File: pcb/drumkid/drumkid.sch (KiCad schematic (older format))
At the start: 21 parts

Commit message: more schematic stuff
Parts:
- added C? (x2): C, symbol Device:C
- added Y?: Crystal, symbol Device:Crystal
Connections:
- net GND: now also C?.1, C?.1
- net at U?.10 (XTAL2/PB7): now also C?.2, Y?.1
- net at U?.9 (XTAL1/PB6): now also C?.2, Y?.2
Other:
- moved on the sheet: RV?
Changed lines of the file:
@@
 L Device:R_POT RV?
 U 1 1 5C8AAE8E
-P 4950 4000
-F 0 "RV?" H 4880 3954 50  0000 R CNN
-F 1 "R_POT" H 4880 4045 50  0000 R CNN
-F 2 "" H 4950 4000 50  0001 C CNN
-F 3 "~" H 4950 4000 50  0001 C CNN
-	1    4950 4000
+P 6200 4550
+F 0 "RV?" H 6130 4504 50  0000 R CNN
+F 1 "R_POT" H 6130 4595 50  0000 R CNN
+F 2 "" H 6200 4550 50  0001 C CNN
+F 3 "~" H 6200 4550 50  0001 C CNN
+	1    6200 4550
 	-1   0    0    1
 $EndComp
@@
 L power:VCC #PWR?
 U 1 1 5C8AB124
-P 4950 3850
-F 0 "#PWR?" H 4950 3700 50  0001 C CNN
-F 1 "VCC" H 4967 4023 50  0000 C CNN
-F 2 "" H 4950 3850 50  0001 C CNN
-F 3 "" H 4950 3850 50  0001 C CNN
-	1    4950 3850
-	1    0    0    -1
-$EndComp
-Wire Wire Line
-	4950 4150 5750 4150
+P 6200 4400
+F 0 "#PWR?" H 6200 4250 50  0001 C CNN
+F 1 "VCC" H 6217 4573 50  0000 C CNN
+F 2 "" H 6200 4400 50  0001 C CNN
+F 3 "" H 6200 4400 50  0001 C CNN
+	1    6200 4400
+	1    0    0    -1
+$EndComp
 Wire Wire Line
 	7650 4150 7650 5500
-Wire Wire Line
-	4800 4000 4450 4000
 $Comp
 L Device:R_POT RV?
@@
 Wire Wire Line
 	5750 3500 5750 4150
-Connection ~ 5750 4150
-Wire Wire Line
-	5750 4150 7650 4150
+Wire Wire Line
+	5750 4150 6600 4150
 Wire Wire Line
 	4450 3100 4450 2850
@@
 Wire Wire Line
 	4500 2450 6050 2450
+$Comp
+L Device:Crystal Y?
+U 1 1 5C8E974C
+P 5000 4000
+F 0 "Y?" H 5000 4268 50  0000 C CNN
+F 1 "Crystal" H 5000 4177 50  0000 C CNN
+F 2 "" H 5000 4000 50  0001 C CNN
+F 3 "~" H 5000 4000 50  0001 C CNN
+	1    5000 4000
+	0    -1   -1   0
+$EndComp
+$Comp
+L Device:C C?
+U 1 1 5C8EA73D
+P 5250 4200
+F 0 "C?" V 4998 4200 50  0000 C CNN
+F 1 "C" V 5089 4200 50  0000 C CNN
+F 2 "" H 5288 4050 50  0001 C CNN
+F 3 "~" H 5250 4200 50  0001 C CNN
+	1    5250 4200
+	0    1    1    0
+$EndComp
+$Comp
+L Device:C C?
+U 1 1 5C8EA7A1
+P 5150 3850
+F 0 "C?" V 4898 3850 50  0000 C CNN
+F 1 "C" V 4989 3850 50  0000 C CNN
+F 2 "" H 5188 3700 50  0001 C CNN
+F 3 "~" H 5150 3850 50  0001 C CNN
+	1    5150 3850
+	0    1    1    0
+$EndComp
+Wire Wire Line
+	4450 3700 5000 3700
+Wire Wire Line
+	5000 3700 5000 3850
+Connection ~ 5000 3850
+Wire Wire Line
+	5000 4150 5000 4200
+Wire Wire Line
+	5000 4200 5100 4200
+Wire Wire Line
+	5000 4200 4650 4200
+Wire Wire Line
+	4650 4200 4650 3800
+Wire Wire Line
+	4650 3800 4450 3800
+Connection ~ 5000 4200
+Wire Wire Line
+	5300 3850 5400 3850
+Wire Wire Line
+	5400 3850 5400 4150
+Wire Wire Line
+	5400 4150 5750 4150
+Connection ~ 5400 4150
+Wire Wire Line
+	5400 4150 5400 4200
+Connection ~ 5750 4150
+Wire Wire Line
+	4450 4000 4600 4000
+Wire Wire Line
+	4600 4000 4600 4550
+Wire Wire Line
+	4600 4550 6050 4550
+Wire Wire Line
+	6200 4700 6600 4700
+Wire Wire Line
+	6600 4700 6600 4150
+Connection ~ 6600 4150
+Wire Wire Line
+	6600 4150 7650 4150
 $EndSCHEMATC

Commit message: omg the circuit works!
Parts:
- added R2: R, symbol Device:R
- gave numbers to parts that had none: 24
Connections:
- net VCC is gone; now on net +5V: C6.1, D1.1 (K), RV2.3, U1.7 (VCC), U2.6 (OUT)
- net at U1.1 (~RESET~/PC6): now also R2.2
- net +5V: now reaches U1.20 (AVCC)
- net +5V: now also R2.1
- net at U2.1 (~SHDN~): now also C1.1, L1.1, SW1.2 (B), U2.5 (LBI)
- no-connect marks 0 -> 13

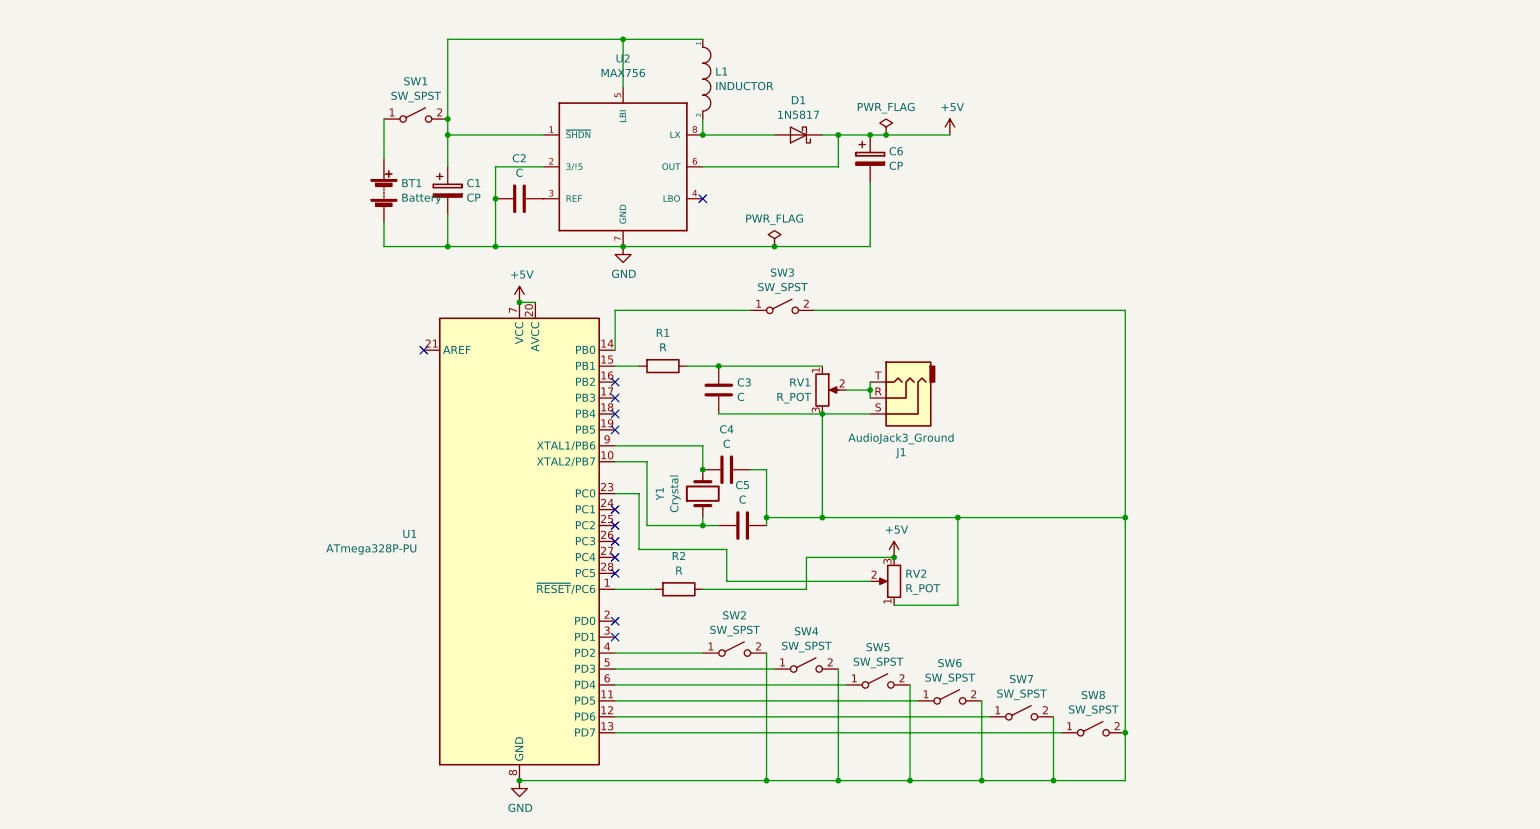
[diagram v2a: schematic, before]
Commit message: added LEDs
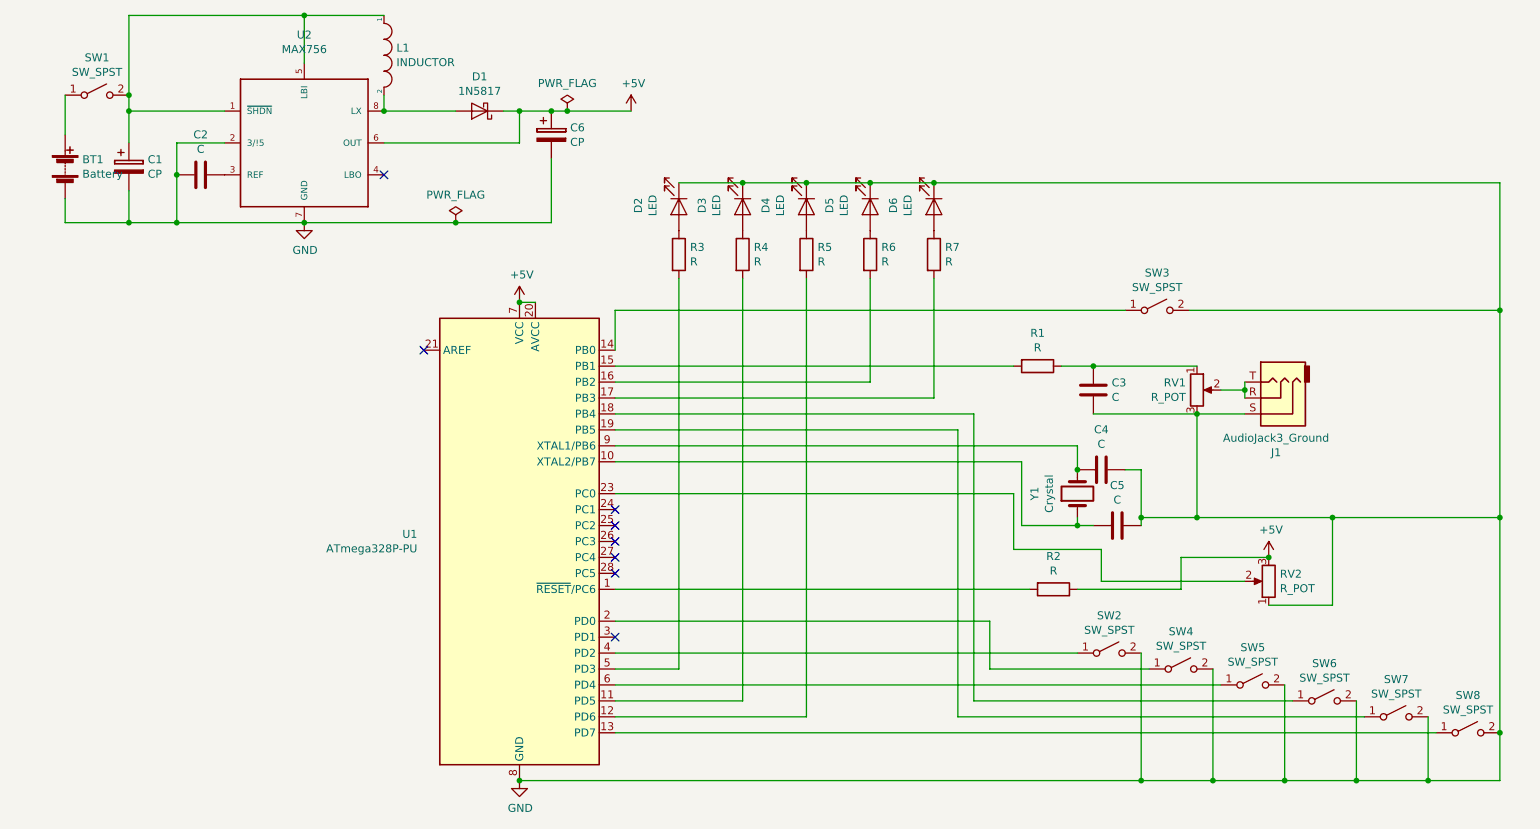
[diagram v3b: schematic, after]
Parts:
- added D2, D3, D4, D5, D6: LED, symbol Device:LED
- added R3, R4, R5, R6, R7: R, symbol Device:R
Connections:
- net GND: now also D2.1 (K), D3.1 (K), D4.1 (K), D5.1 (K), D6.1 (K)
- net at U1.11 (PD5): now also R4.2; no longer SW6.1 (A)
- net at U1.12 (PD6): now also R5.2; no longer SW7.1 (A)
- net at U1.16 (PB2): now also R6.2
- net at U1.17 (PB3): now also R7.2
- net at U1.18 (PB4): now also SW6.1 (A)
- net at U1.19 (PB5): now also SW7.1 (A)
- net at U1.2 (PD0): now also SW4.1 (A)
- net at U1.5 (PD3): now also R3.2; no longer SW4.1 (A)
- new net: D5.2 (A), R6.1
- new net: D2.2 (A), R3.1
- new net: D3.2 (A), R4.1
- new net: D4.2 (A), R5.1
- new net: D6.2 (A), R7.1
- no-connect marks 13 -> 8
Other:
- moved on the sheet: BT1, C1, C2, C3, C4, C5, C6, D1, J1, L1, R1, R2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

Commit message: added component values
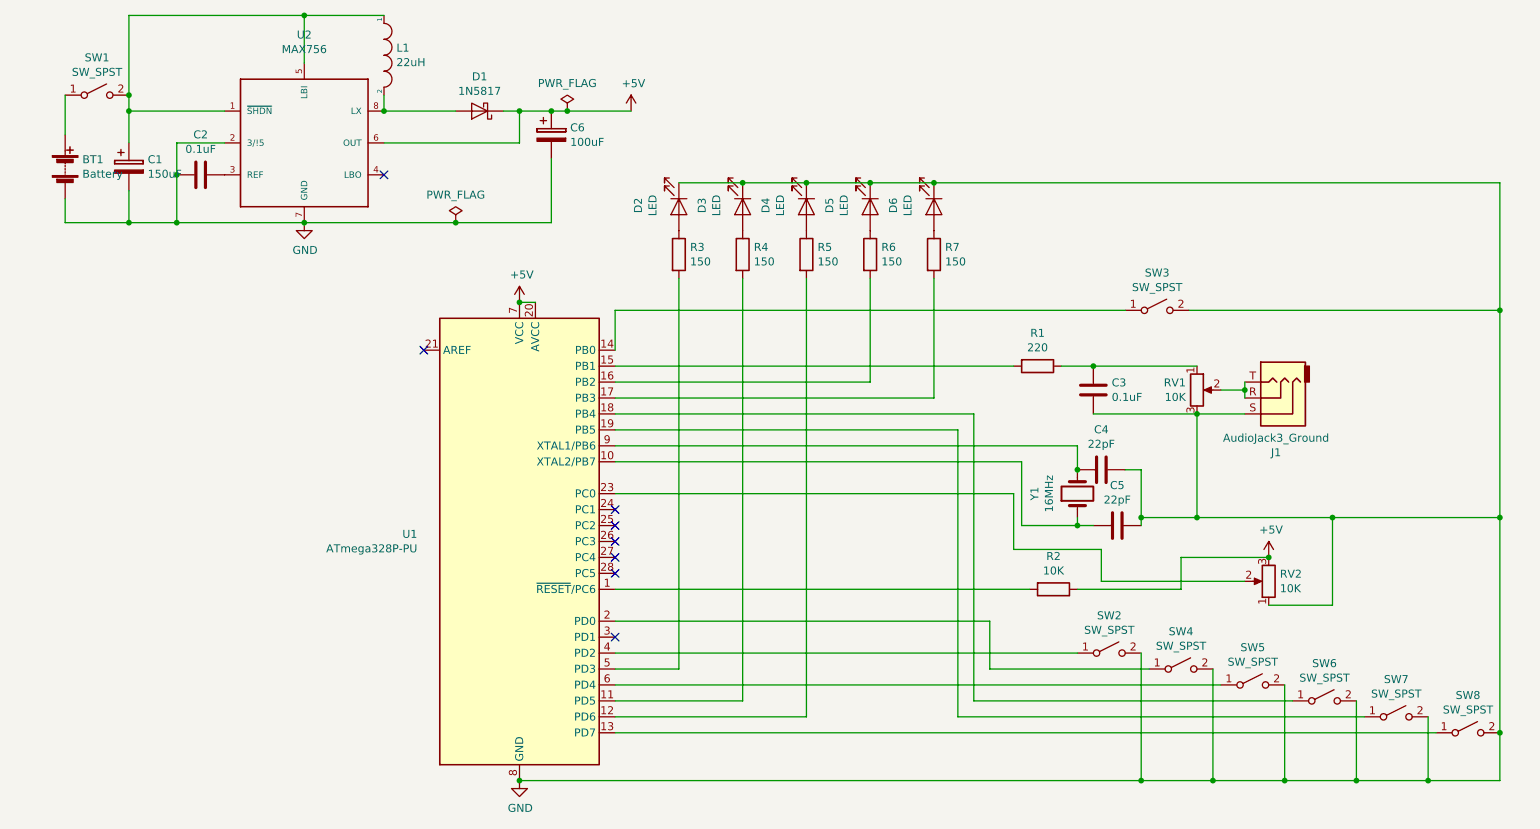
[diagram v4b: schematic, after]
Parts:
- C1: value CP -> 150uF
- C2, C3: value C -> 0.1uF
- C4, C5: value C -> 22pF
- C6: value CP -> 100uF
- L1: value INDUCTOR -> 22uH
- R1: value R -> 220
- R2: value R -> 10K
- R3, R4, R5, R6, R7: value R -> 150
- RV1, RV2: value R_POT -> 10K
- Y1: value Crystal -> 16MHz
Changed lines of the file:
@@
 P 7100 3200
 F 0 "R1" V 6893 3200 50  0000 C CNN
-F 1 "R" V 6984 3200 50  0000 C CNN
+F 1 "220" V 6984 3200 50  0000 C CNN
 F 2 "" V 7030 3200 50  0001 C CNN
 F 3 "~" H 7100 3200 50  0001 C CNN
@@
 P 7450 3350
 F 0 "C3" H 7335 3304 50  0000 R CNN
-F 1 "C" H 7335 3395 50  0000 R CNN
+F 1 "0.1uF" H 7335 3395 50  0000 R CNN
 F 2 "" H 7488 3200 50  0001 C CNN
 F 3 "~" H 7450 3350 50  0001 C CNN
@@
 P 8550 4550
 F 0 "RV2" H 8480 4504 50  0000 R CNN
-F 1 "R_POT" H 8480 4595 50  0000 R CNN
+F 1 "10K" H 8480 4595 50  0000 R CNN
 F 2 "" H 8550 4550 50  0001 C CNN
 F 3 "~" H 8550 4550 50  0001 C CNN
@@
 P 8100 3350
 F 0 "RV1" H 8030 3396 50  0000 R CNN
-F 1 "R_POT" H 8030 3305 50  0000 R CNN
+F 1 "10K" H 8030 3305 50  0000 R CNN
 F 2 "" H 8100 3350 50  0001 C CNN
 F 3 "~" H 8100 3350 50  0001 C CNN
@@
 P 1850 2000
 F 0 "C2" V 1598 2000 50  0000 C CNN
-F 1 "C" V 1689 2000 50  0000 C CNN
+F 1 "0.1uF" V 1689 2000 50  0000 C CNN
 F 2 "" H 1888 1850 50  0001 C CNN
 F 3 "~" H 1850 2000 50  0001 C CNN
@@
 P 3000 1250
 F 0 "L1" V 2954 1328 50  0000 L CNN
-F 1 "INDUCTOR" V 3045 1328 50  0000 L CNN
+F 1 "22uH" V 3045 1328 50  0000 L CNN
 F 2 "" H 3000 1250 50  0001 C CNN
 F 3 "~" H 3000 1250 50  0001 C CNN
@@
 P 4050 1750
 F 0 "C6" H 4168 1796 50  0000 L CNN
-F 1 "CP" H 4168 1705 50  0000 L CNN
+F 1 "100uF" H 4168 1705 50  0000 L CNN
 F 2 "" H 4088 1600 50  0001 C CNN
 F 3 "~" H 4050 1750 50  0001 C CNN
@@
 P 7350 4000
 F 0 "Y1" H 7350 4268 50  0000 C CNN
-F 1 "Crystal" H 7350 4177 50  0000 C CNN
+F 1 "16MHz" H 7350 4177 50  0000 C CNN
 F 2 "" H 7350 4000 50  0001 C CNN
 F 3 "~" H 7350 4000 50  0001 C CNN
@@
 P 7600 4200
 F 0 "C5" V 7348 4200 50  0000 C CNN
-F 1 "C" V 7439 4200 50  0000 C CNN
+F 1 "22pF" V 7439 4200 50  0000 C CNN
 F 2 "" H 7638 4050 50  0001 C CNN
 F 3 "~" H 7600 4200 50  0001 C CNN
@@
 P 7500 3850
 F 0 "C4" V 7248 3850 50  0000 C CNN
-F 1 "C" V 7339 3850 50  0000 C CNN
+F 1 "22pF" V 7339 3850 50  0000 C CNN
 F 2 "" H 7538 3700 50  0001 C CNN
 F 3 "~" H 7500 3850 50  0001 C CNN
@@
 P 1400 1950
 F 0 "C1" H 1518 1996 50  0000 L CNN
-F 1 "CP" H 1518 1905 50  0000 L CNN
+F 1 "150uF" H 1518 1905 50  0000 L CNN
 F 2 "" H 1438 1800 50  0001 C CNN
 F 3 "~" H 1400 1950 50  0001 C CNN
@@
 P 7200 4600
 F 0 "R2" V 6993 4600 50  0000 C CNN
-F 1 "R" V 7084 4600 50  0000 C CNN
+F 1 "10K" V 7084 4600 50  0000 C CNN
 F 2 "" V 7130 4600 50  0001 C CNN
 F 3 "~" H 7200 4600 50  0001 C CNN
@@
 P 4850 2500
 F 0 "R3" H 4920 2546 50  0000 L CNN
-F 1 "R" H 4920 2455 50  0000 L CNN
+F 1 "150" H 4920 2455 50  0000 L CNN
 F 2 "" V 4780 2500 50  0001 C CNN
 F 3 "~" H 4850 2500 50  0001 C CNN
@@
 P 5250 2500
 F 0 "R4" H 5320 2546 50  0000 L CNN
-F 1 "R" H 5320 2455 50  0000 L CNN
+F 1 "150" H 5320 2455 50  0000 L CNN
 F 2 "" V 5180 2500 50  0001 C CNN
 F 3 "~" H 5250 2500 50  0001 C CNN
@@
 P 5650 2500
 F 0 "R5" H 5720 2546 50  0000 L CNN
-F 1 "R" H 5720 2455 50  0000 L CNN
+F 1 "150" H 5720 2455 50  0000 L CNN
 F 2 "" V 5580 2500 50  0001 C CNN
 F 3 "~" H 5650 2500 50  0001 C CNN
@@
 P 6050 2500
 F 0 "R6" H 6120 2546 50  0000 L CNN
-F 1 "R" H 6120 2455 50  0000 L CNN
+F 1 "150" H 6120 2455 50  0000 L CNN
 F 2 "" V 5980 2500 50  0001 C CNN
 F 3 "~" H 6050 2500 50  0001 C CNN
@@
 P 6450 2500
 F 0 "R7" H 6520 2546 50  0000 L CNN
-F 1 "R" H 6520 2455 50  0000 L CNN
+F 1 "150" H 6520 2455 50  0000 L CNN
 F 2 "" V 6380 2500 50  0001 C CNN
 F 3 "~" H 6450 2500 50  0001 C CNN

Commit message: assigned a bunch of footprints but missing some
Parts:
- BT1: footprint (none) -> Connector_PinHeader_2.54mm:PinHeader_1x02_P2.54mm_Vertical
- C1, C6: footprint (none) -> Capacitor_THT:CP_Radial_D6.3mm_P2.50mm
- C2, C3, C4, C5: footprint (none) -> Capacitor_THT:C_Disc_D3.4mm_W2.1mm_P2.50mm
- D2, D3, D4, D5, D6: footprint (none) -> LED_THT:LED_D5.0mm
- L1: footprint (none) -> Inductor_THT:L_Radial_D6.0mm_P4.00mm
- R1, R2, R3, R4, R5, R6, R7: footprint (none) -> Resistor_THT:R_Axial_DIN0207_L6.3mm_D2.5mm_P10.16mm_Horizontal
- RV1, RV2: footprint (none) -> Potentiometer_THT:Potentiometer_Bourns_PTV09A-1_Single_Vertical
- U2: footprint SO08 -> Package_DIP:DIP-8_W7.62mm_Socket
- Y1: footprint (none) -> Crystal:Crystal_HC49-4H_Vertical
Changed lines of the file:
@@
 F 0 "R1" V 6893 3200 50  0000 C CNN
 F 1 "220" V 6984 3200 50  0000 C CNN
-F 2 "" V 7030 3200 50  0001 C CNN
+F 2 "Resistor_THT:R_Axial_DIN0207_L6.3mm_D2.5mm_P10.16mm_Horizontal" V 7030 3200 50  0001 C CNN
 F 3 "~" H 7100 3200 50  0001 C CNN
 	1    7100 3200
@@
 F 0 "C3" H 7335 3304 50  0000 R CNN
 F 1 "0.1uF" H 7335 3395 50  0000 R CNN
-F 2 "" H 7488 3200 50  0001 C CNN
+F 2 "Capacitor_THT:C_Disc_D3.4mm_W2.1mm_P2.50mm" H 7488 3200 50  0001 C CNN
 F 3 "~" H 7450 3350 50  0001 C CNN
 	1    7450 3350
@@
 F 0 "RV2" H 8480 4504 50  0000 R CNN
 F 1 "10K" H 8480 4595 50  0000 R CNN
-F 2 "" H 8550 4550 50  0001 C CNN
+F 2 "Potentiometer_THT:Potentiometer_Bourns_PTV09A-1_Single_Vertical" H 8550 4550 50  0001 C CNN
 F 3 "~" H 8550 4550 50  0001 C CNN
 	1    8550 4550
@@
 F 0 "RV1" H 8030 3396 50  0000 R CNN
 F 1 "10K" H 8030 3305 50  0000 R CNN
-F 2 "" H 8100 3350 50  0001 C CNN
+F 2 "Potentiometer_THT:Potentiometer_Bourns_PTV09A-1_Single_Vertical" H 8100 3350 50  0001 C CNN
 F 3 "~" H 8100 3350 50  0001 C CNN
 	1    8100 3350
@@
 F 0 "BT1" H 1108 1996 50  0000 L CNN
 F 1 "Battery" H 1108 1905 50  0000 L CNN
-F 2 "" V 1000 2010 50  0001 C CNN
+F 2 "Connector_PinHeader_2.54mm:PinHeader_1x02_P2.54mm_Vertical" V 1000 2010 50  0001 C CNN
 F 3 "~" V 1000 2010 50  0001 C CNN
 	1    1000 1950
@@
 F 0 "U2" H 2500 2478 50  0000 C CNN
 F 1 "MAX756" H 2500 2387 50  0000 C CNN
-F 2 "SO08" H 2500 1800 50  0001 L BNN
+F 2 "Package_DIP:DIP-8_W7.62mm_Socket" H 2500 1800 50  0001 L BNN
 F 3 "Unavailable" H 2500 1800 50  0001 L BNN
 F 4 "None" H 2500 1800 50  0001 L BNN "Field4"
@@
 F 0 "C2" V 1598 2000 50  0000 C CNN
 F 1 "0.1uF" V 1689 2000 50  0000 C CNN
-F 2 "" H 1888 1850 50  0001 C CNN
+F 2 "Capacitor_THT:C_Disc_D3.4mm_W2.1mm_P2.50mm" H 1888 1850 50  0001 C CNN
 F 3 "~" H 1850 2000 50  0001 C CNN
 	1    1850 2000
@@
 F 0 "L1" V 2954 1328 50  0000 L CNN
 F 1 "22uH" V 3045 1328 50  0000 L CNN
-F 2 "" H 3000 1250 50  0001 C CNN
+F 2 "Inductor_THT:L_Radial_D6.0mm_P4.00mm" H 3000 1250 50  0001 C CNN
 F 3 "~" H 3000 1250 50  0001 C CNN
 	1    3000 1250
@@
 F 0 "C6" H 4168 1796 50  0000 L CNN
 F 1 "100uF" H 4168 1705 50  0000 L CNN
-F 2 "" H 4088 1600 50  0001 C CNN
+F 2 "Capacitor_THT:CP_Radial_D6.3mm_P2.50mm" H 4088 1600 50  0001 C CNN
 F 3 "~" H 4050 1750 50  0001 C CNN
 	1    4050 1750
@@
 F 0 "Y1" H 7350 4268 50  0000 C CNN
 F 1 "16MHz" H 7350 4177 50  0000 C CNN
-F 2 "" H 7350 4000 50  0001 C CNN
+F 2 "Crystal:Crystal_HC49-4H_Vertical" H 7350 4000 50  0001 C CNN
 F 3 "~" H 7350 4000 50  0001 C CNN
 	1    7350 4000
@@
 F 0 "C5" V 7348 4200 50  0000 C CNN
 F 1 "22pF" V 7439 4200 50  0000 C CNN
-F 2 "" H 7638 4050 50  0001 C CNN
+F 2 "Capacitor_THT:C_Disc_D3.4mm_W2.1mm_P2.50mm" H 7638 4050 50  0001 C CNN
 F 3 "~" H 7600 4200 50  0001 C CNN
 	1    7600 4200
@@
 F 0 "C4" V 7248 3850 50  0000 C CNN
 F 1 "22pF" V 7339 3850 50  0000 C CNN
-F 2 "" H 7538 3700 50  0001 C CNN
+F 2 "Capacitor_THT:C_Disc_D3.4mm_W2.1mm_P2.50mm" H 7538 3700 50  0001 C CNN
 F 3 "~" H 7500 3850 50  0001 C CNN
 	1    7500 3850
@@
 F 0 "C1" H 1518 1996 50  0000 L CNN
 F 1 "150uF" H 1518 1905 50  0000 L CNN
-F 2 "" H 1438 1800 50  0001 C CNN
+F 2 "Capacitor_THT:CP_Radial_D6.3mm_P2.50mm" H 1438 1800 50  0001 C CNN
 F 3 "~" H 1400 1950 50  0001 C CNN
 	1    1400 1950
@@
 F 0 "R2" V 6993 4600 50  0000 C CNN
 F 1 "10K" V 7084 4600 50  0000 C CNN
-F 2 "" V 7130 4600 50  0001 C CNN
+F 2 "Resistor_THT:R_Axial_DIN0207_L6.3mm_D2.5mm_P10.16mm_Horizontal" V 7130 4600 50  0001 C CNN
 F 3 "~" H 7200 4600 50  0001 C CNN
 	1    7200 4600
@@
 F 0 "D5" H 6042 1945 50  0000 C CNN
 F 1 "LED" H 6042 2036 50  0000 C CNN
-F 2 "" H 6050 2200 50  0001 C CNN
+F 2 "LED_THT:LED_D5.0mm" H 6050 2200 50  0001 C CNN
 F 3 "~" H 6050 2200 50  0001 C CNN
 	1    6050 2200
@@
 F 0 "D2" H 4842 1945 50  0000 C CNN
 F 1 "LED" H 4842 2036 50  0000 C CNN
-F 2 "" H 4850 2200 50  0001 C CNN
+F 2 "LED_THT:LED_D5.0mm" H 4850 2200 50  0001 C CNN
 F 3 "~" H 4850 2200 50  0001 C CNN
 	1    4850 2200
@@
 F 0 "D3" H 5242 1945 50  0000 C CNN
 F 1 "LED" H 5242 2036 50  0000 C CNN
-F 2 "" H 5250 2200 50  0001 C CNN
+F 2 "LED_THT:LED_D5.0mm" H 5250 2200 50  0001 C CNN
 F 3 "~" H 5250 2200 50  0001 C CNN
 	1    5250 2200
@@
 F 0 "D4" H 5642 1945 50  0000 C CNN
 F 1 "LED" H 5642 2036 50  0000 C CNN
-F 2 "" H 5650 2200 50  0001 C CNN
+F 2 "LED_THT:LED_D5.0mm" H 5650 2200 50  0001 C CNN
 F 3 "~" H 5650 2200 50  0001 C CNN
 	1    5650 2200
@@
 F 0 "R3" H 4920 2546 50  0000 L CNN
 F 1 "150" H 4920 2455 50  0000 L CNN
-F 2 "" V 4780 2500 50  0001 C CNN
+F 2 "Resistor_THT:R_Axial_DIN0207_L6.3mm_D2.5mm_P10.16mm_Horizontal" V 4780 2500 50  0001 C CNN
 F 3 "~" H 4850 2500 50  0001 C CNN
 	1    4850 2500
@@
 F 0 "R4" H 5320 2546 50  0000 L CNN
 F 1 "150" H 5320 2455 50  0000 L CNN
-F 2 "" V 5180 2500 50  0001 C CNN
+F 2 "Resistor_THT:R_Axial_DIN0207_L6.3mm_D2.5mm_P10.16mm_Horizontal" V 5180 2500 50  0001 C CNN
 F 3 "~" H 5250 2500 50  0001 C CNN
 	1    5250 2500
@@
 F 0 "R5" H 5720 2546 50  0000 L CNN
 F 1 "150" H 5720 2455 50  0000 L CNN
-F 2 "" V 5580 2500 50  0001 C CNN
+F 2 "Resistor_THT:R_Axial_DIN0207_L6.3mm_D2.5mm_P10.16mm_Horizontal" V 5580 2500 50  0001 C CNN
 F 3 "~" H 5650 2500 50  0001 C CNN
 	1    5650 2500
@@
 F 0 "R6" H 6120 2546 50  0000 L CNN
 F 1 "150" H 6120 2455 50  0000 L CNN
-F 2 "" V 5980 2500 50  0001 C CNN
+F 2 "Resistor_THT:R_Axial_DIN0207_L6.3mm_D2.5mm_P10.16mm_Horizontal" V 5980 2500 50  0001 C CNN
 F 3 "~" H 6050 2500 50  0001 C CNN
 	1    6050 2500
@@
 F 0 "D6" H 6442 1945 50  0000 C CNN
 F 1 "LED" H 6442 2036 50  0000 C CNN
-F 2 "" H 6450 2200 50  0001 C CNN
+F 2 "LED_THT:LED_D5.0mm" H 6450 2200 50  0001 C CNN
 F 3 "~" H 6450 2200 50  0001 C CNN
 	1    6450 2200
@@
 F 0 "R7" H 6520 2546 50  0000 L CNN
 F 1 "150" H 6520 2455 50  0000 L CNN
-F 2 "" V 6380 2500 50  0001 C CNN
+F 2 "Resistor_THT:R_Axial_DIN0207_L6.3mm_D2.5mm_P10.16mm_Horizontal" V 6380 2500 50  0001 C CNN
 F 3 "~" H 6450 2500 50  0001 C CNN
 	1    6450 2500
